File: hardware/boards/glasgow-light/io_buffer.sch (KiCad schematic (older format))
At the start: 63 parts, among them J2 IDC-Header_2x5_P2.54mm, J3 IDC-Header_2x5_P2.54mm, U11 TPS73101DBV, U12 INA180A2, U16 SN74LVC1T45DCKR, U17 SN74LVC1T45DCKR, U18 SN74LVC1T45DCKR, U19 PCA6408APW, U19 SN74LVC1T45DCKR, U20 SN74LVC1T45DCKR, U21 SN74LVC1T45DCKR, U5 SN74LVC1T45DCKR, U6 SN74LVC1T45DCKR

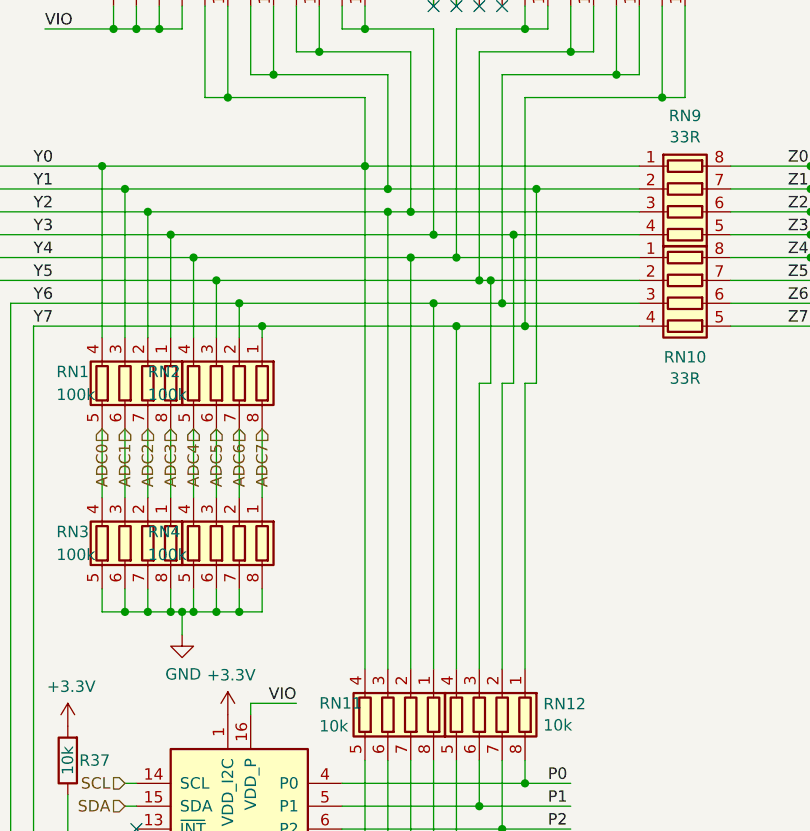
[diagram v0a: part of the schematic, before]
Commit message: swap some pins
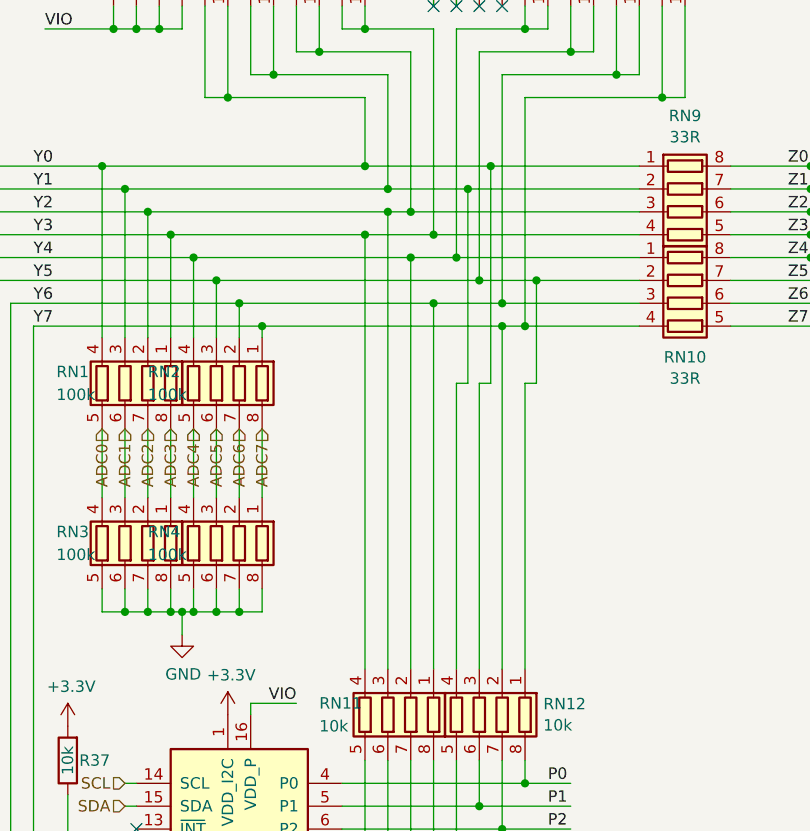
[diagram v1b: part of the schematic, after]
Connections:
- wire segments 354 -> 355
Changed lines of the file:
@@
 Connection ~ 7650 2550
 Connection ~ 7550 2450
-Wire Wire Line
-	7450 2350 7800 2350
 Connection ~ 7450 2350
 Connection ~ 7350 2250
@@
 	9750 2250 9600 2250
 Wire Wire Line
-	7650 2550 7700 2550
-Wire Wire Line
 	9700 2650 9700 2350
 Wire Wire Line
@@
 	9150 4250 9150 5000
 Wire Wire Line
-	7250 2150 7900 2150
+	7250 2150 7600 2150
 Wire Wire Line
 	7350 2250 8350 2250
-Wire Wire Line
-	7150 2050 8350 2050
 $Comp
 L Device:R_Pack04 RN3
@@
 Connection ~ 6300 2350
 Wire Wire Line
-	6300 2350 7450 2350
+	6300 2350 7150 2350
 Wire Wire Line
 	6400 2800 6400 2450
@@
 	6700 2800 6700 2750
 Connection ~ 6700 2750
-Wire Wire Line
-	6700 2750 7550 2750
 Wire Wire Line
 	10700 1450 10950 1450
@@
 	7250 2250 7350 2250
 Wire Wire Line
-	7150 4250 7150 2050
-Wire Wire Line
 	7850 4250 7850 3000
 Wire Wire Line
 	7850 3000 7900 3000
 Wire Wire Line
-	7900 3000 7900 2150
-Connection ~ 7900 2150
-Wire Wire Line
-	7900 2150 8350 2150
-Wire Wire Line
-	7750 4250 7750 3000
-Wire Wire Line
-	7750 3000 7800 3000
-Wire Wire Line
-	7800 3000 7800 2350
-Connection ~ 7800 2350
-Wire Wire Line
-	7800 2350 8350 2350
-Wire Wire Line
 	7650 4250 7650 3000
 Wire Wire Line
 	7650 3000 7700 3000
 Wire Wire Line
-	7700 3000 7700 2550
-Connection ~ 7700 2550
-Wire Wire Line
-	7700 2550 8350 2550
-Wire Wire Line
-	7550 4250 7550 2750
-Connection ~ 7550 2750
-Wire Wire Line
-	7550 2750 7850 2750
+	6700 2750 7750 2750
+Wire Wire Line
+	7550 4250 7550 3000
+Wire Wire Line
+	7550 3000 7600 3000
+Wire Wire Line
+	7650 2550 7900 2550
+Wire Wire Line
+	7150 2050 7700 2050
+Wire Wire Line
+	7600 3000 7600 2150
+Connection ~ 7600 2150
+Wire Wire Line
+	7600 2150 8350 2150
+Wire Wire Line
+	7700 3000 7700 2050
+Connection ~ 7700 2050
+Wire Wire Line
+	7700 2050 8350 2050
+Wire Wire Line
+	7150 4250 7150 2350
+Connection ~ 7150 2350
+Wire Wire Line
+	7150 2350 7450 2350
+Wire Wire Line
+	7900 3000 7900 2550
+Connection ~ 7900 2550
+Wire Wire Line
+	7900 2550 8350 2550
+Wire Wire Line
+	7450 2350 8350 2350
+Connection ~ 7750 2750
+Wire Wire Line
+	7750 2750 7850 2750
+Wire Wire Line
+	7750 2750 7750 4250
 $EndSCHEMATC

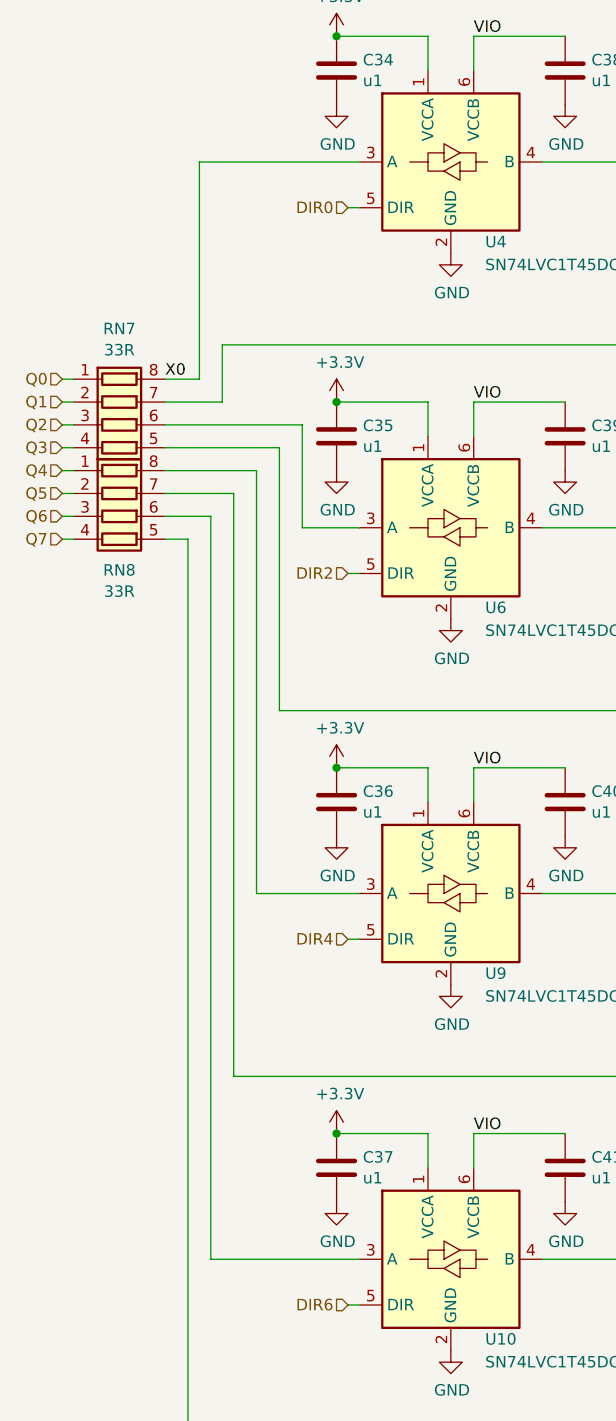
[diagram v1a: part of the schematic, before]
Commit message: route resistor arrays between FPGA and buffers
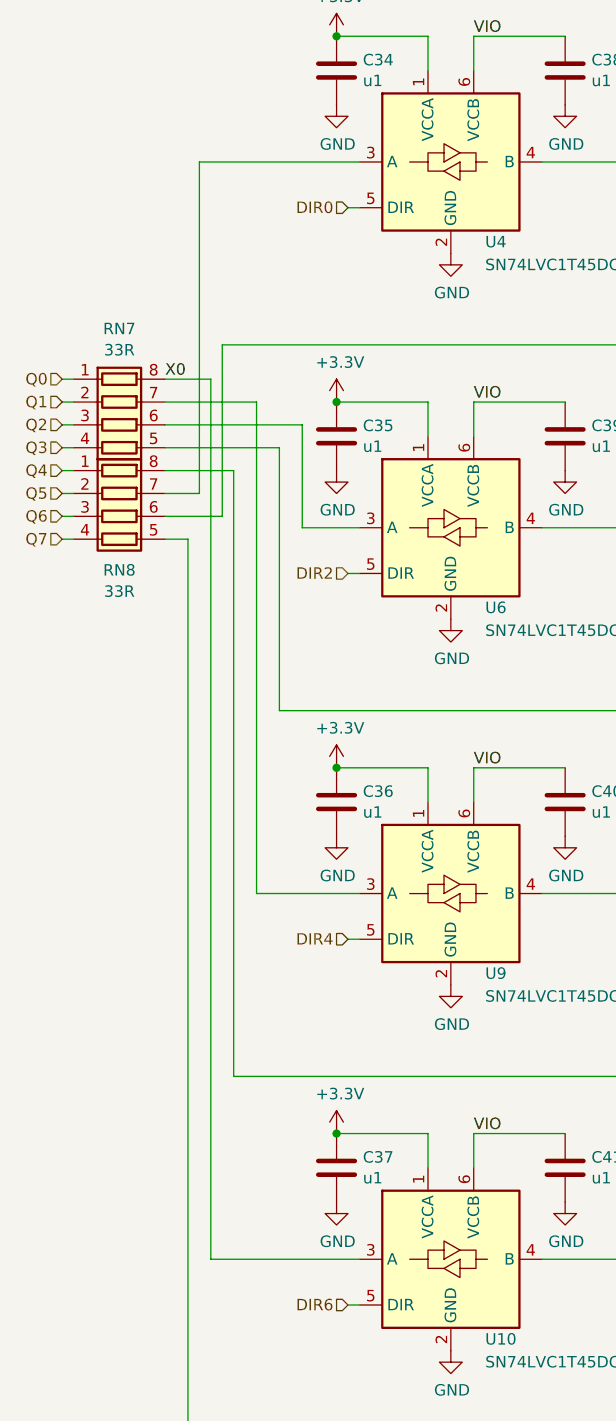
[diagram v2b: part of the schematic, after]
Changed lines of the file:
@@
 	850  3100 800  3100
 Wire Wire Line
-	1250 2400 1400 2400
-Wire Wire Line
-	1400 2400 1400 1450
-Wire Wire Line
 	1400 1450 2100 1450
 Wire Wire Line
-	1250 2500 1500 2500
-Wire Wire Line
-	1500 2500 1500 2250
-Wire Wire Line
 	1500 2250 3850 2250
 Wire Wire Line
@@
 	1750 3850 3850 3850
 Wire Wire Line
-	1250 2800 1650 2800
-Wire Wire Line
-	1650 2800 1650 4650
-Wire Wire Line
 	1650 4650 2100 4650
 Wire Wire Line
-	1250 2900 1550 2900
-Wire Wire Line
-	1550 2900 1550 5450
-Wire Wire Line
 	1550 5450 3850 5450
-Wire Wire Line
-	1250 3000 1450 3000
-Wire Wire Line
-	1450 3000 1450 6250
 Wire Wire Line
 	1450 6250 2100 6250
@@
 Wire Wire Line
 	7750 2750 7750 4250
+Wire Wire Line
+	1650 2500 1650 4650
+Wire Wire Line
+	1250 2500 1650 2500
+Wire Wire Line
+	1450 2400 1450 6250
+Wire Wire Line
+	1550 2800 1250 2800
+Wire Wire Line
+	1550 2800 1550 5450
+Wire Wire Line
+	1400 2900 1250 2900
+Wire Wire Line
+	1250 2400 1450 2400
+Wire Wire Line
+	1400 2900 1400 1450
+Wire Wire Line
+	1500 2250 1500 3000
+Wire Wire Line
+	1500 3000 1250 3000
 $EndSCHEMATC

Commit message: add some test points
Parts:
- added TP22: 3V3, TestPoint:TestPoint_Pad_D1.0mm, symbol Connector:TestPoint
- added TP23: VCURR, TestPoint:TestPoint_Pad_D1.0mm, symbol Connector:TestPoint
- added TP24, TP31: GND, TestPoint:TestPoint_Pad_D1.0mm, symbol Connector:TestPoint
- added TP25: VIO, TestPoint:TestPoint_Pad_D1.0mm, symbol Connector:TestPoint
- added TP26: Y5, TestPoint:TestPoint_Pad_D1.0mm, symbol Connector:TestPoint
- added TP27: Y6, TestPoint:TestPoint_Pad_D1.0mm, symbol Connector:TestPoint
- added TP28: Y7, TestPoint:TestPoint_Pad_D1.0mm, symbol Connector:TestPoint
- added TP29: ADC7, TestPoint:TestPoint_Pad_D1.0mm, symbol Connector:TestPoint
- added TP30: ADC5, TestPoint:TestPoint_Pad_D1.0mm, symbol Connector:TestPoint
- added TP?: P5, TestPoint:TestPoint_Pad_D1.0mm, symbol Connector:TestPoint
- added TP?: P7, TestPoint:TestPoint_Pad_D1.0mm, symbol Connector:TestPoint
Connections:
- wire segments 355 -> 363
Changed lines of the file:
@@
 Wire Wire Line
 	1500 3000 1250 3000
+$Comp
+L Connector:TestPoint TP?
+U 1 1 60282967
+P 10450 4200
+AR Path="/60282967" Ref="TP?"  Part="1"
+AR Path="/5C7B59B0/5C9E337E/60282967" Ref="TP23"  Part="1"
+AR Path="/5C7B59B0/5C9E338E/60282967" Ref="TP?"  Part="1"
+AR Path="/5FFD4B90/60282967" Ref="TP?"  Part="1"
+AR Path="/5FFD4BA1/60282967" Ref="TP?"  Part="1"
+F 0 "TP23" V 10350 4350 50  0000 C CNN
+F 1 "VCURR" V 10554 4274 50  0001 C CNN
+F 2 "TestPoint:TestPoint_Pad_D1.0mm" H 10650 4200 50  0001 C CNN
+F 3 "~" H 10650 4200 50  0001 C CNN
+	1    10450 4200
+	0    1    1    0
+$EndComp
+$Comp
+L Connector:TestPoint TP?
+U 1 1 602A4934
+P 10900 3900
+AR Path="/602A4934" Ref="TP?"  Part="1"
+AR Path="/5C7B59B0/5C9E337E/602A4934" Ref="TP24"  Part="1"
+AR Path="/5C7B59B0/5C9E338E/602A4934" Ref="TP?"  Part="1"
+AR Path="/5FFD4B90/602A4934" Ref="TP?"  Part="1"
+AR Path="/5FFD4BA1/602A4934" Ref="TP?"  Part="1"
+F 0 "TP24" V 10800 4050 50  0000 C CNN
+F 1 "GND" V 11004 3974 50  0001 C CNN
+F 2 "TestPoint:TestPoint_Pad_D1.0mm" H 11100 3900 50  0001 C CNN
+F 3 "~" H 11100 3900 50  0001 C CNN
+	1    10900 3900
+	0    1    1    0
+$EndComp
+$Comp
+L Connector:TestPoint TP?
+U 1 1 602A7D69
+P 10200 3200
+AR Path="/602A7D69" Ref="TP?"  Part="1"
+AR Path="/5C7B59B0/5C9E337E/602A7D69" Ref="TP22"  Part="1"
+AR Path="/5C7B59B0/5C9E338E/602A7D69" Ref="TP?"  Part="1"
+AR Path="/5FFD4B90/602A7D69" Ref="TP?"  Part="1"
+AR Path="/5FFD4BA1/602A7D69" Ref="TP?"  Part="1"
+F 0 "TP22" V 10100 3350 50  0000 C CNN
+F 1 "3V3" V 10304 3274 50  0001 C CNN
+F 2 "TestPoint:TestPoint_Pad_D1.0mm" H 10400 3200 50  0001 C CNN
+F 3 "~" H 10400 3200 50  0001 C CNN
+	1    10200 3200
+	0    -1   -1   0
+$EndComp
+Wire Wire Line
+	10450 4200 10400 4200
+Wire Wire Line
+	10900 3900 10850 3900
+Wire Wire Line
+	10850 3900 10850 3700
+Wire Wire Line
+	10200 3200 10300 3200
+Connection ~ 10300 3200
+$Comp
+L Connector:TestPoint TP?
+U 1 1 60327AE0
+P 10200 6350
+AR Path="/60327AE0" Ref="TP?"  Part="1"
+AR Path="/5C7B59B0/5C9E337E/60327AE0" Ref="TP25"  Part="1"
+AR Path="/5C7B59B0/5C9E338E/60327AE0" Ref="TP?"  Part="1"
+AR Path="/5FFD4B90/60327AE0" Ref="TP?"  Part="1"
+AR Path="/5FFD4BA1/60327AE0" Ref="TP?"  Part="1"
+F 0 "TP25" V 10100 6500 50  0000 C CNN
+F 1 "VIO" V 10304 6424 50  0001 C CNN
+F 2 "TestPoint:TestPoint_Pad_D1.0mm" H 10400 6350 50  0001 C CNN
+F 3 "~" H 10400 6350 50  0001 C CNN
+	1    10200 6350
+	0    1    1    0
+$EndComp
+Text Label 10050 6350 0    50   ~ 0
+VIO
+Wire Wire Line
+	10050 6350 10200 6350
+$Comp
+L Connector:TestPoint TP?
+U 1 1 603F6E25
+P 6700 2000
+AR Path="/603F6E25" Ref="TP?"  Part="1"
+AR Path="/5C7B59B0/5C9E337E/603F6E25" Ref="TP28"  Part="1"
+AR Path="/5C7B59B0/5C9E338E/603F6E25" Ref="TP?"  Part="1"
+AR Path="/5FFD4B90/603F6E25" Ref="TP?"  Part="1"
+AR Path="/5FFD4BA1/603F6E25" Ref="TP?"  Part="1"
+F 0 "TP28" V 6800 2150 50  0000 C CNN
+F 1 "Y7" V 6804 2074 50  0001 C CNN
+F 2 "TestPoint:TestPoint_Pad_D1.0mm" H 6900 2000 50  0001 C CNN
+F 3 "~" H 6900 2000 50  0001 C CNN
+	1    6700 2000
+	1    0    0    -1
+$EndComp
+$Comp
+L Connector:TestPoint TP?
+U 1 1 603F9CA2
+P 6600 2000
+AR Path="/603F9CA2" Ref="TP?"  Part="1"
+AR Path="/5C7B59B0/5C9E337E/603F9CA2" Ref="TP27"  Part="1"
+AR Path="/5C7B59B0/5C9E338E/603F9CA2" Ref="TP?"  Part="1"
+AR Path="/5FFD4B90/603F9CA2" Ref="TP?"  Part="1"
+AR Path="/5FFD4BA1/603F9CA2" Ref="TP?"  Part="1"
+F 0 "TP27" H 6600 2200 50  0000 C CNN
+F 1 "Y6" V 6704 2074 50  0001 C CNN
+F 2 "TestPoint:TestPoint_Pad_D1.0mm" H 6800 2000 50  0001 C CNN
+F 3 "~" H 6800 2000 50  0001 C CNN
+	1    6600 2000
+	1    0    0    -1
+$EndComp
+Wire Wire Line
+	6500 2000 6500 2550
+Wire Wire Line
+	6600 2000 6600 2650
+Wire Wire Line
+	6700 2000 6700 2750
+$Comp
+L Connector:TestPoint TP?
+U 1 1 6047373A
+P 6950 3050
+AR Path="/6047373A" Ref="TP?"  Part="1"
+AR Path="/5C7B59B0/5C9E337E/6047373A" Ref="TP29"  Part="1"
+AR Path="/5C7B59B0/5C9E338E/6047373A" Ref="TP?"  Part="1"
+AR Path="/5FFD4B90/6047373A" Ref="TP?"  Part="1"
+AR Path="/5FFD4BA1/6047373A" Ref="TP?"  Part="1"
+F 0 "TP29" V 6850 3200 50  0000 C CNN
+F 1 "ADC7" V 7054 3124 50  0001 C CNN
+F 2 "TestPoint:TestPoint_Pad_D1.0mm" H 7150 3050 50  0001 C CNN
+F 3 "~" H 7150 3050 50  0001 C CNN
+	1    6950 3050
+	1    0    0    -1
+$EndComp
+$Comp
+L Connector:TestPoint TP?
+U 1 1 60474338
+P 6950 3500
+AR Path="/60474338" Ref="TP?"  Part="1"
+AR Path="/5C7B59B0/5C9E337E/60474338" Ref="TP30"  Part="1"
+AR Path="/5C7B59B0/5C9E338E/60474338" Ref="TP?"  Part="1"
+AR Path="/5FFD4B90/60474338" Ref="TP?"  Part="1"
+AR Path="/5FFD4BA1/60474338" Ref="TP?"  Part="1"
+F 0 "TP30" V 6850 3650 50  0000 C CNN
+F 1 "ADC5" V 7054 3574 50  0001 C CNN
+F 2 "TestPoint:TestPoint_Pad_D1.0mm" H 7150 3500 50  0001 C CNN
+F 3 "~" H 7150 3500 50  0001 C CNN
+	1    6950 3500
+	1    0    0    -1
+$EndComp
+Text HLabel 6950 3050 3    50   Input ~ 0
+ADC7
+Text HLabel 6950 3500 3    50   Input ~ 0
+ADC5
+$Comp
+L Connector:TestPoint TP?
+U 1 1 6049E506
+P 6950 3950
+AR Path="/6049E506" Ref="TP?"  Part="1"
+AR Path="/5C7B59B0/5C9E337E/6049E506" Ref="TP31"  Part="1"
+AR Path="/5C7B59B0/5C9E338E/6049E506" Ref="TP?"  Part="1"
+AR Path="/5FFD4B90/6049E506" Ref="TP?"  Part="1"
+AR Path="/5FFD4BA1/6049E506" Ref="TP?"  Part="1"
+F 0 "TP31" V 6850 4100 50  0000 C CNN
+F 1 "GND" V 7054 4024 50  0001 C CNN
+F 2 "TestPoint:TestPoint_Pad_D1.0mm" H 7150 3950 50  0001 C CNN
+F 3 "~" H 7150 3950 50  0001 C CNN
+	1    6950 3950
+	1    0    0    -1
+$EndComp
+$Comp
+L power:GND #PWR?
+U 1 1 6049EEC3
+P 6950 3950
+AR Path="/5AF7D604/6049EEC3" Ref="#PWR?"  Part="1"
+AR Path="/5AFBDC9E/6049EEC3" Ref="#PWR?"  Part="1"
+AR Path="/5C7B59B0/5C9E337E/6049EEC3" Ref="#PWR0131"  Part="1"
+AR Path="/5C7B59B0/5C9E338E/6049EEC3" Ref="#PWR?"  Part="1"
+AR Path="/5FFD4B90/6049EEC3" Ref="#PWR?"  Part="1"
+AR Path="/5FFD4BA1/6049EEC3" Ref="#PWR?"  Part="1"
+F 0 "#PWR0131" H 6950 3700 50  0001 C CNN
+F 1 "GND" H 6955 3777 50  0000 C CNN
+F 2 "" H 6950 3950 50  0001 C CNN
+F 3 "" H 6950 3950 50  0001 C CNN
+	1    6950 3950
+	1    0    0    -1
+$EndComp
+$Comp
+L Connector:TestPoint TP?
+U 1 1 603FA8E6
+P 6500 2000
+AR Path="/603FA8E6" Ref="TP?"  Part="1"
+AR Path="/5C7B59B0/5C9E337E/603FA8E6" Ref="TP26"  Part="1"
+AR Path="/5C7B59B0/5C9E338E/603FA8E6" Ref="TP?"  Part="1"
+AR Path="/5FFD4B90/603FA8E6" Ref="TP?"  Part="1"
+AR Path="/5FFD4BA1/603FA8E6" Ref="TP?"  Part="1"
+F 0 "TP26" V 6400 2150 50  0000 C CNN
+F 1 "Y5" V 6604 2074 50  0001 C CNN
+F 2 "TestPoint:TestPoint_Pad_D1.0mm" H 6700 2000 50  0001 C CNN
+F 3 "~" H 6700 2000 50  0001 C CNN
+	1    6500 2000
+	1    0    0    -1
+$EndComp
+$Comp
+L Connector:TestPoint TP?
+U 1 1 604DF2C1
+P 8050 5250
+AR Path="/604DF2C1" Ref="TP?"  Part="1"
+AR Path="/5C7B59B0/5C9E337E/604DF2C1" Ref="TP?"  Part="1"
+AR Path="/5C7B59B0/5C9E338E/604DF2C1" Ref="TP?"  Part="1"
+AR Path="/5FFD4B90/604DF2C1" Ref="TP?"  Part="1"
+AR Path="/5FFD4BA1/604DF2C1" Ref="TP?"  Part="1"
+F 0 "TP?" V 7950 5400 50  0000 C CNN
+F 1 "P5" V 8154 5324 50  0001 C CNN
+F 2 "TestPoint:TestPoint_Pad_D1.0mm" H 8250 5250 50  0001 C CNN
+F 3 "~" H 8250 5250 50  0001 C CNN
+	1    8050 5250
+	0    1    1    0
+$EndComp
+$Comp
+L Connector:TestPoint TP?
+U 1 1 604E0486
+P 8050 5450
+AR Path="/604E0486" Ref="TP?"  Part="1"
+AR Path="/5C7B59B0/5C9E337E/604E0486" Ref="TP?"  Part="1"
+AR Path="/5C7B59B0/5C9E338E/604E0486" Ref="TP?"  Part="1"
+AR Path="/5FFD4B90/604E0486" Ref="TP?"  Part="1"
+AR Path="/5FFD4BA1/604E0486" Ref="TP?"  Part="1"
+F 0 "TP?" V 7950 5600 50  0000 C CNN
+F 1 "P7" V 8154 5524 50  0001 C CNN
+F 2 "TestPoint:TestPoint_Pad_D1.0mm" H 8250 5450 50  0001 C CNN
+F 3 "~" H 8250 5450 50  0001 C CNN
+	1    8050 5450
+	0    1    1    0
+$EndComp
 $EndSCHEMATC
